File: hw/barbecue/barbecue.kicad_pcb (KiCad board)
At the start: 2 copper layers, 124.5 x 54.8 mm, 52 parts, among them J1 47590-0001, J10 TFT, J11 SDCard, J2 Screw_Terminal_01x02, J3 bootsel, J4 gnd clk swd, J5 +pwm3-, J6 R_{ntc}, J7 +pwm2-, J8 +pwm1-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

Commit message: Small board fixes
Signed-off-by: Jan Hamal Dvořák <mordae@anilinux.org>
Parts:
- moved J11 0.48 mm to (98.5, 59.5)
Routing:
- net +5V: track 27.1 -> 36.7 mm
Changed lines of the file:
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@@
   )
   (footprint "Connector_PinSocket_2.54mm:PinSocket_1x04_P2.54mm_Vertical" (layer "F.Cu")
-    (at 98.19 59.09)
+    (at 98.5 59.46)
     (descr "Through hole straight socket strip, 1x04, 2.54mm pitch, single row (from Kicad 4.0.7), script generated")
     (tags "Through hole socket strip THT 1x04 2.54mm single row")
@@
   (via (at 129 55) (size 0.6) (drill 0.3) (layers "F.Cu" "B.Cu") (net 4))
   (via (at 120 55) (size 0.6) (drill 0.3) (layers "F.Cu" "B.Cu") (net 4))
-  (segment (start 129 55) (end 129 57) (width 0.4) (layer "B.Cu") (net 4))
-  (segment (start 129 57) (end 129.95 57.95) (width 0.4) (layer "B.Cu") (net 4))
+  (segment (start 129 55) (end 129 58) (width 0.4) (layer "B.Cu") (net 4))
+  (segment (start 129.9 58) (end 129.95 57.95) (width 0.4) (layer "B.Cu") (net 4))
   (segment (start 120 55) (end 120 58) (width 0.4) (layer "B.Cu") (net 4))
+  (segment (start 120 58) (end 129 58) (width 0.4) (layer "B.Cu") (net 4))
   (segment (start 111.77 58) (end 111 57.23) (width 0.4) (layer "B.Cu") (net 4))
   (segment (start 120 58) (end 111.77 58) (width 0.4) (layer "B.Cu") (net 4))
+  (segment (start 129 58) (end 129.9 58) (width 0.4) (layer "B.Cu") (net 4))
   (segment (start 111 55) (end 111 57.23) (width 0.4) (layer "B.Cu") (net 4))
   (segment (start 62.975 64.35) (end 62.975 63.625) (width 0.2) (layer "F.Cu") (net 5))

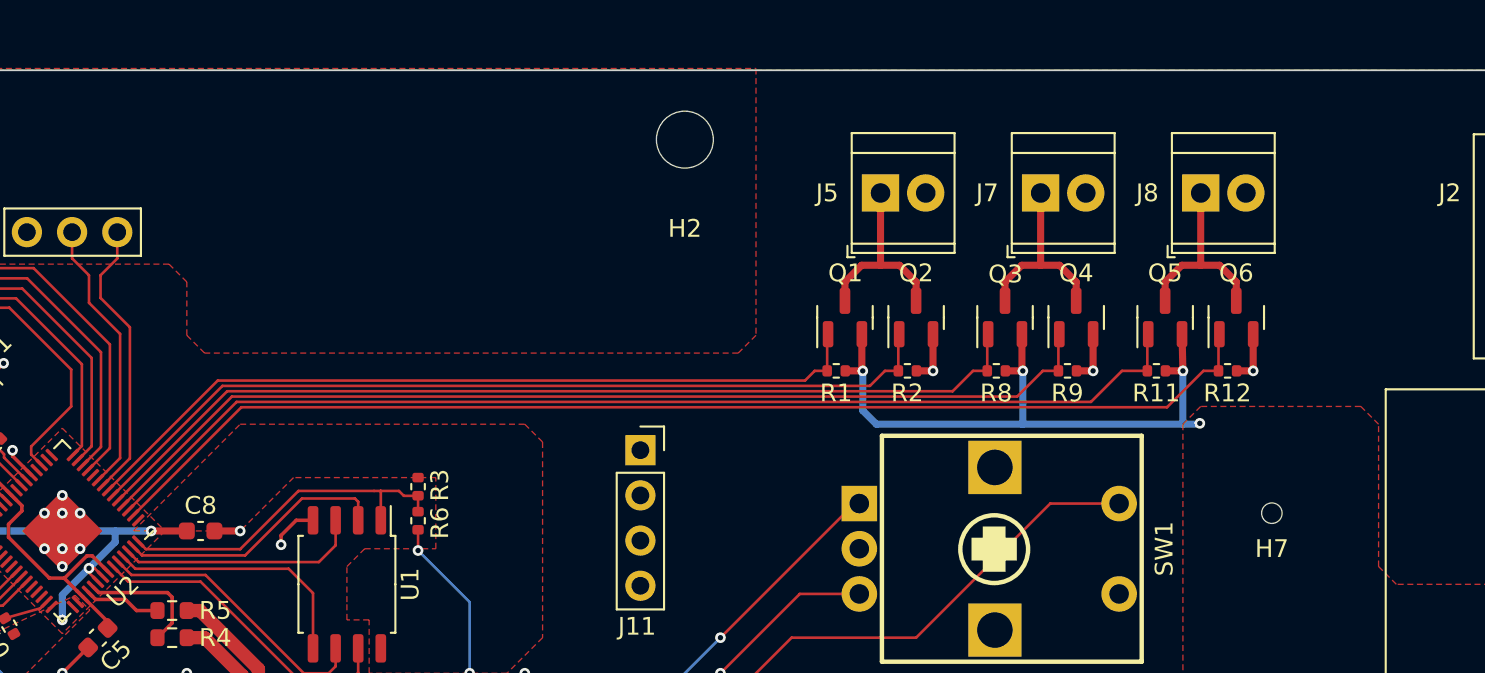
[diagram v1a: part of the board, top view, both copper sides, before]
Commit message: Fix board PWM outputs
Signed-off-by: Jan Hamal Dvořák <mordae@anilinux.org>
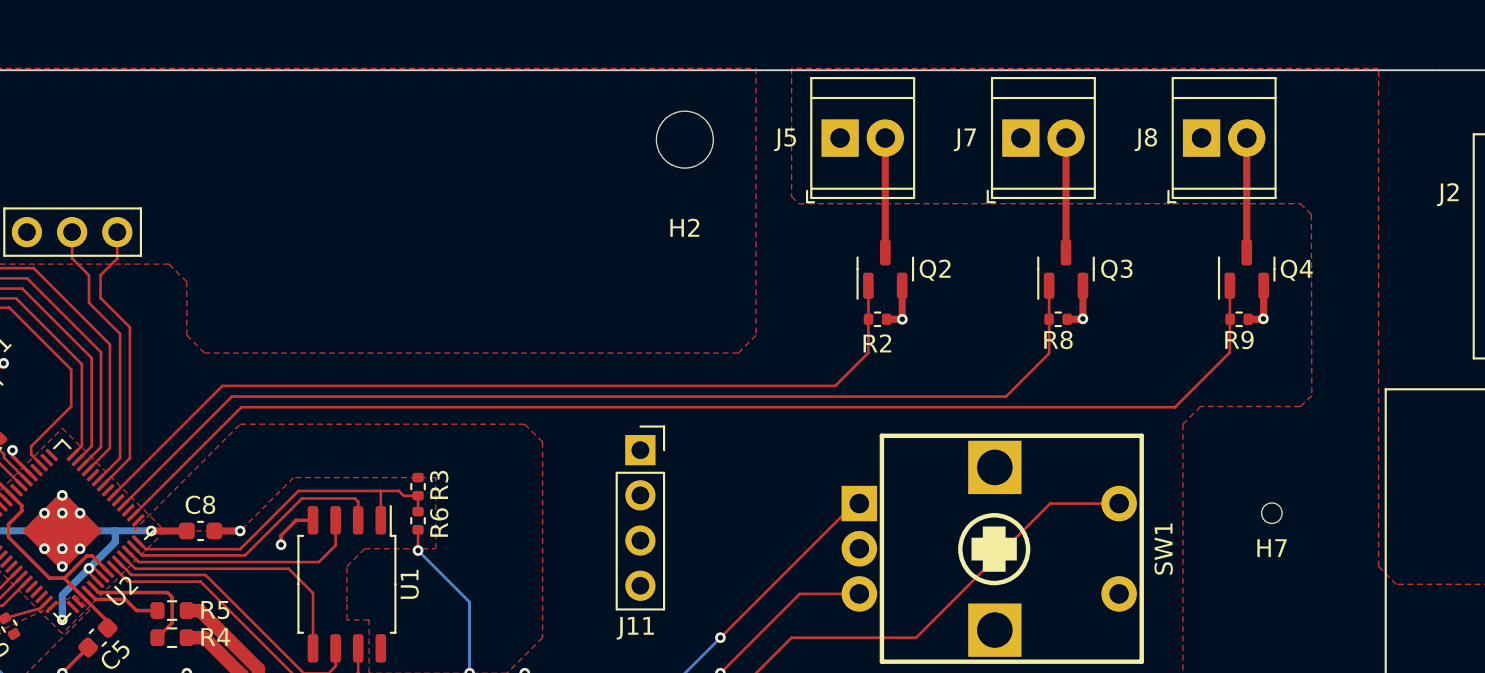
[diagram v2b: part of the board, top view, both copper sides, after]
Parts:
- removed Q1, Q5: AO3401A, Package_TO_SOT_SMD:SOT-23
- removed Q6: AO3400A, Package_TO_SOT_SMD:SOT-23
- removed R1, R11, R12: 47k, Resistor_SMD:R_0402_1005Metric
- J7: value +pwm2- -> +pwm3-
- J8: value +pwm1- -> +pwm3-
- Q3: value AO3401A -> AO3400A
- moved R9 10.1 mm to (132.2, 52.1)
- moved Q4 9.97 mm to (132.6, 49.3)
- moved R8 4.53 mm to (122.0, 52.1), turned to 0 degrees
- moved Q3 4.38 mm to (122.4, 49.3)
- moved J5 3.84 mm to (109.7, 41.9)
- moved R2 3.35 mm to (111.8, 52.1)
- moved J7 3.28 mm to (119.9, 41.9)
- moved Q2 3.23 mm to (112.3, 49.3)
- moved J8 3.09 mm to (130.0, 41.9)
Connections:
- net /pwm3a renamed /PWM_{3}
- J5 pad 1: Net-(J5-Pin_1) -> +5V
- J5 pad 2: GND -> Net-(J5-Pin_2)
- J7 pad 1: Net-(J7-Pin_1) -> +5V
- J7 pad 2: GND -> Net-(J7-Pin_2)
- J8 pad 1: Net-(J8-Pin_1) -> +5V
- J8 pad 2: GND -> Net-(J8-Pin_2)
- Q2 pad 3: Net-(J5-Pin_1) -> Net-(J5-Pin_2)
- Q3 pad 1: /pwm2b -> /PWM_{2}
- Q3 pad 2: +5V -> GND
- Q3 pad 3: Net-(J7-Pin_1) -> Net-(J7-Pin_2)
- Q4 pad 1: /pwm2a -> /PWM_{1}
- Q4 pad 3: Net-(J7-Pin_1) -> Net-(J8-Pin_2)
- R8 pad 1: +5V -> /PWM_{2}
- R8 pad 2: /pwm2b -> GND
- R9 pad 1: /pwm2a -> /PWM_{1}
- U2 pad 2: /pwm1a -> /PWM_{1}
- U2 pad 3: /pwm1b -> unconnected-(U2-GPIO1)
- U2 pad 4: /pwm2a -> /PWM_{2}
- U2 pad 5: /pwm2b -> unconnected-(U2-GPIO3)
- U2 pad 7: /pwm3b -> unconnected-(U2-GPIO5)
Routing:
- net /PWM_{1}: track 0.00 -> 69.2 mm
- net /pwm1a: track 66.5 -> 0.00 mm
- net /pwm1b: track 62.6 -> 0.00 mm
- net /PWM_{2}: track 0.00 -> 59.4 mm
- net /pwm2a: track 57.8 -> 0.00 mm
- net /pwm2b: track 53.9 -> 0.00 mm
- net /pwm3b: track 45.3 -> 0.00 mm
- net +5V: track 36.7 -> 0.00 mm, vias 4 -> 0
- net Net-(J8-Pin_1): track 11.0 -> 0.00 mm
- net Net-(J7-Pin_1): track 11.0 -> 0.00 mm
- net Net-(J5-Pin_1): track 11.0 -> 0.00 mm
- net Net-(J8-Pin_2): track 0.00 -> 6.43 mm
- net Net-(J7-Pin_2): track 0.00 -> 6.43 mm
- net Net-(J5-Pin_2): track 0.00 -> 6.43 mm
- net GND: track 49.5 -> 48.8 mm

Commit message: Version 1.1 as sent to manufacturing
Signed-off-by: Jan Hamal Dvořák <mordae@anilinux.org>
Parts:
- removed J10: TFT, Connector_PinSocket_2.54mm:PinSocket_1x11_P2.54mm_Vertical
- removed J11: SDCard, Connector_PinSocket_2.54mm:PinSocket_1x04_P2.54mm_Vertical
- removed J9: OLED, Connector_PinSocket_2.54mm:PinSocket_1x04_P2.54mm_Vertical
- added C11: 22u, Capacitor_SMD:C_0603_1608Metric, F.Cu at (135.9, 59.7)
- added C12: 22u, Capacitor_SMD:C_0603_1608Metric, F.Cu at (115.3, 78.1)
- added H8: Tooling, Barbecue:ToolingHole, F.Cu at (160.0, 53.3)
- added U4: ILI9225-MOD, Barbecue:ILI9225-MOD, B.Cu at (129.5, 73.7)
- J5: value +pwm3- -> +HEAT-
- J6: value R_{ntc} -> NTC
- J7: value +pwm3- -> +FAN1-
- J8: value +pwm3- -> +FAN2-
- R10: footprint Resistor_SMD:R_0402_1005Metric -> Resistor_SMD:R_0603_1608Metric
- SW1: moved to B.Cu
- moved PS1 97.4 mm to (55.9, 66.0)
- moved J2 97.3 mm to (50.9, 53.3)
- moved H6 87.0 mm to (43.2, 48.3)
- moved J6 85.3 mm to (121.9, 53.3), turned to 0 degrees
- moved C2 82.8 mm to (134.8, 84.9)
- moved C1 78.0 mm to (131.4, 85.1), turned to 135 degrees
- moved Y1 77.6 mm to (132.7, 83.2), turned to 135 degrees
- moved C6 76.0 mm to (134.0, 78.9), turned to -45 degrees
- moved R7 73.7 mm to (133.0, 79.6), turned to 135 degrees
- moved C7 71.6 mm to (129.5, 67.2), turned to 45 degrees
- moved H3 70.9 mm to (160.0, 48.3)
- moved R10 67.5 mm to (130.6, 68.3), turned to 45 degrees
- moved J4 66.5 mm to (129.5, 96.5)
- moved U2 63.6 mm to (128.7, 74.5), turned to 45 degrees
- moved H2 63.2 mm to (38.1, 48.3)
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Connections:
- Q2 pad 1: /PWM_{3} -> /heat
- Q3 pad 1: /PWM_{2} -> /fan1
- Q4 pad 1: /PWM_{1} -> /fan2
- R2 pad 1: /PWM_{3} -> /heat
- R8 pad 1: /PWM_{2} -> /fan1
- R9 pad 1: /PWM_{1} -> /fan2
- U2 pad 11: /tft_rst -> unconnected-(U2-GPIO8-Pad11)
- U2 pad 12: /tft_cs -> /re_a
- U2 pad 13: /tft_sclk -> /re_b
- U2 pad 14: /tft_mosi -> /re_sw
- U2 pad 17: /tft_rs -> unconnected-(U2-GPIO14-Pad17)
- U2 pad 2: /PWM_{1} -> unconnected-(U2-GPIO0-Pad2)
- U2 pad 3: unconnected-(U2-GPIO1) -> /sd_cs
- U2 pad 32: unconnected-(U2-GPIO21) -> /tft_cs
- U2 pad 34: unconnected-(U2-GPIO22) -> /tft_sck
- U2 pad 35: /re_sw -> /tft_mosi
- U2 pad 36: /re_b -> /tft_rs
- U2 pad 37: /re_a -> /tft_rst
- U2 pad 38: unconnected-(U2-GPIO26_ADC0) -> /fan2
- U2 pad 39: unconnected-(U2-GPIO27_ADC1) -> /fan1
- U2 pad 4: /PWM_{2} -> /sd_sck
- U2 pad 40: unconnected-(U2-GPIO28_ADC2) -> /tsense
- U2 pad 41: /tsense -> /heat
- U2 pad 5: unconnected-(U2-GPIO3) -> /sd_mosi
- U2 pad 6: /PWM_{3} -> /sd_miso
- U2 pad 8: /sda -> unconnected-(U2-GPIO6-Pad8)
- U2 pad 9: /scl -> unconnected-(U2-GPIO7-Pad9)
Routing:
- net /PWM_{1}: track 69.2 -> 0.00 mm
- net /PWM_{2}: track 59.4 -> 0.00 mm
- net /PWM_{3}: track 49.6 -> 0.00 mm
- net /tft_sclk: track 45.8 -> 0.00 mm
- net /sd_mosi: track 0.00 -> 32.6 mm, vias 0 -> 1
- net /sd_cs: track 0.00 -> 32.3 mm
- net /sd_miso: track 0.00 -> 31.1 mm
- net /sd_sck: track 0.00 -> 30.9 mm
- net /tft_sck: track 0.00 -> 26.4 mm
- net /heat: track 0.00 -> 24.4 mm
- net /re_sw: track 81.3 -> 60.4 mm, vias 2 -> 0
- net +5V: track 0.00 -> 18.2 mm
- net /re_b: track 61.9 -> 44.1 mm, vias 2 -> 0
- net /swdclk: track 42.1 -> 25.1 mm, vias 2 -> 0
- net /swdio: track 41.2 -> 24.7 mm, vias 2 -> 0
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- added copper zone on F.Cu, net GND
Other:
- board size 124.5 x 54.8 mm -> 127 x 55.9 mm
- board text added: "+3V3"
- board text added: "+5V"
- board text added: "Barbecue 1.1"
- board text added: "porucha.net"
- board text removed: "L N"
- board text removed: "N L"
